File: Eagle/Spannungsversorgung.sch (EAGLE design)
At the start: 2 parts

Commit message: Added PinHeads to the Eagle file
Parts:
- added JP1, JP2: (no value), pinhead:PINHD-1X22
- added U1: ESP32-S2-SAOLA-1R, ESP32-S2-SAOLA-1R:ESP32-S2-SAOLA-1R
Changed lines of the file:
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@@
 <setting verticaltext="up"/>
 </settings>
-<grid distance="0.1" unitdist="inch" unit="mil" style="lines" multiple="1" display="yes" altdistance="0.01" altunitdist="inch" altunit="inch"/>
+<grid distance="0.1" unitdist="inch" unit="inch" style="lines" multiple="1" display="no" altdistance="0.01" altunitdist="inch" altunit="inch"/>
 <layers>
 <layer number="1" name="Top" color="4" fill="1" visible="no" active="no"/>
@@
 <part name="GND2" library="supply1" library_urn="urn:adsk.eagle:library:371" deviceset="GND" device=""/>
 <part name="FRAME1" library="frames" library_urn="urn:adsk.eagle:library:229" deviceset="A4L-LOC" device=""/>
+<part name="JP1" library="pinhead" library_urn="urn:adsk.eagle:library:325" deviceset="PINHD-1X22" device="" package3d_urn="urn:adsk.eagle:package:22442/3"/>
+<part name="JP2" library="pinhead" library_urn="urn:adsk.eagle:library:325" deviceset="PINHD-1X22" device="" package3d_urn="urn:adsk.eagle:package:22442/3"/>
+<part name="U1" library="ESP32-S2-SAOLA-1R" deviceset="ESP32-S2-SAOLA-1R" device=""/>
+<part name="FRAME2" library="frames" library_urn="urn:adsk.eagle:library:229" deviceset="A4L-LOC" device=""/>
+<part name="FRAME3" library="frames" library_urn="urn:adsk.eagle:library:229" deviceset="A4L-LOC" device=""/>
 </parts>
 <sheets>
+<sheet>
+<description>PINs</description>
+<plain>
+</plain>
+<instances>
+<instance part="JP1" gate="A" x="20.32" y="55.88" smashed="yes">
+<attribute name="NAME" x="13.97" y="84.455" size="1.778" layer="95"/>
+<attribute name="VALUE" x="13.97" y="22.86" size="1.778" layer="96"/>
+</instance>
+<instance part="JP2" gate="A" x="50.8" y="55.88" smashed="yes">
+<attribute name="NAME" x="44.45" y="84.455" size="1.778" layer="95"/>
+<attribute name="VALUE" x="44.45" y="22.86" size="1.778" layer="96"/>
+</instance>
+<instance part="FRAME2" gate="G$1" x="0" y="0" smashed="yes">
+<attribute name="DRAWING_NAME" x="217.17" y="15.24" size="2.54" layer="94"/>
+<attribute name="LAST_DATE_TIME" x="217.17" y="10.16" size="2.286" layer="94"/>
+<attribute name="SHEET" x="230.505" y="5.08" size="2.54" layer="94"/>
+</instance>
+</instances>
+<busses>
+</busses>
+<nets>
+</nets>
+</sheet>
 <sheet>
 <description>Spannungsregler</description>
@@
 </nets>
 </sheet>
+<sheet>
+<description>Verschiedenes</description>
+<plain>
+</plain>
+<instances>
+<instance part="U1" gate="G$1" x="73.66" y="58.42" smashed="yes">
+<attribute name="NAME" x="58.42" y="93.98" size="1.778" layer="95" align="top-left"/>
+<attribute name="VALUE" x="58.42" y="22.86" size="1.778" layer="96"/>
+</instance>
+<instance part="FRAME3" gate="G$1" x="0" y="0" smashed="yes">
+<attribute name="DRAWING_NAME" x="217.17" y="15.24" size="2.54" layer="94"/>
+<attribute name="LAST_DATE_TIME" x="217.17" y="10.16" size="2.286" layer="94"/>
+<attribute name="SHEET" x="230.505" y="5.08" size="2.54" layer="94"/>
+</instance>
+</instances>
+<busses>
+</busses>
+<nets>
+</nets>
+</sheet>

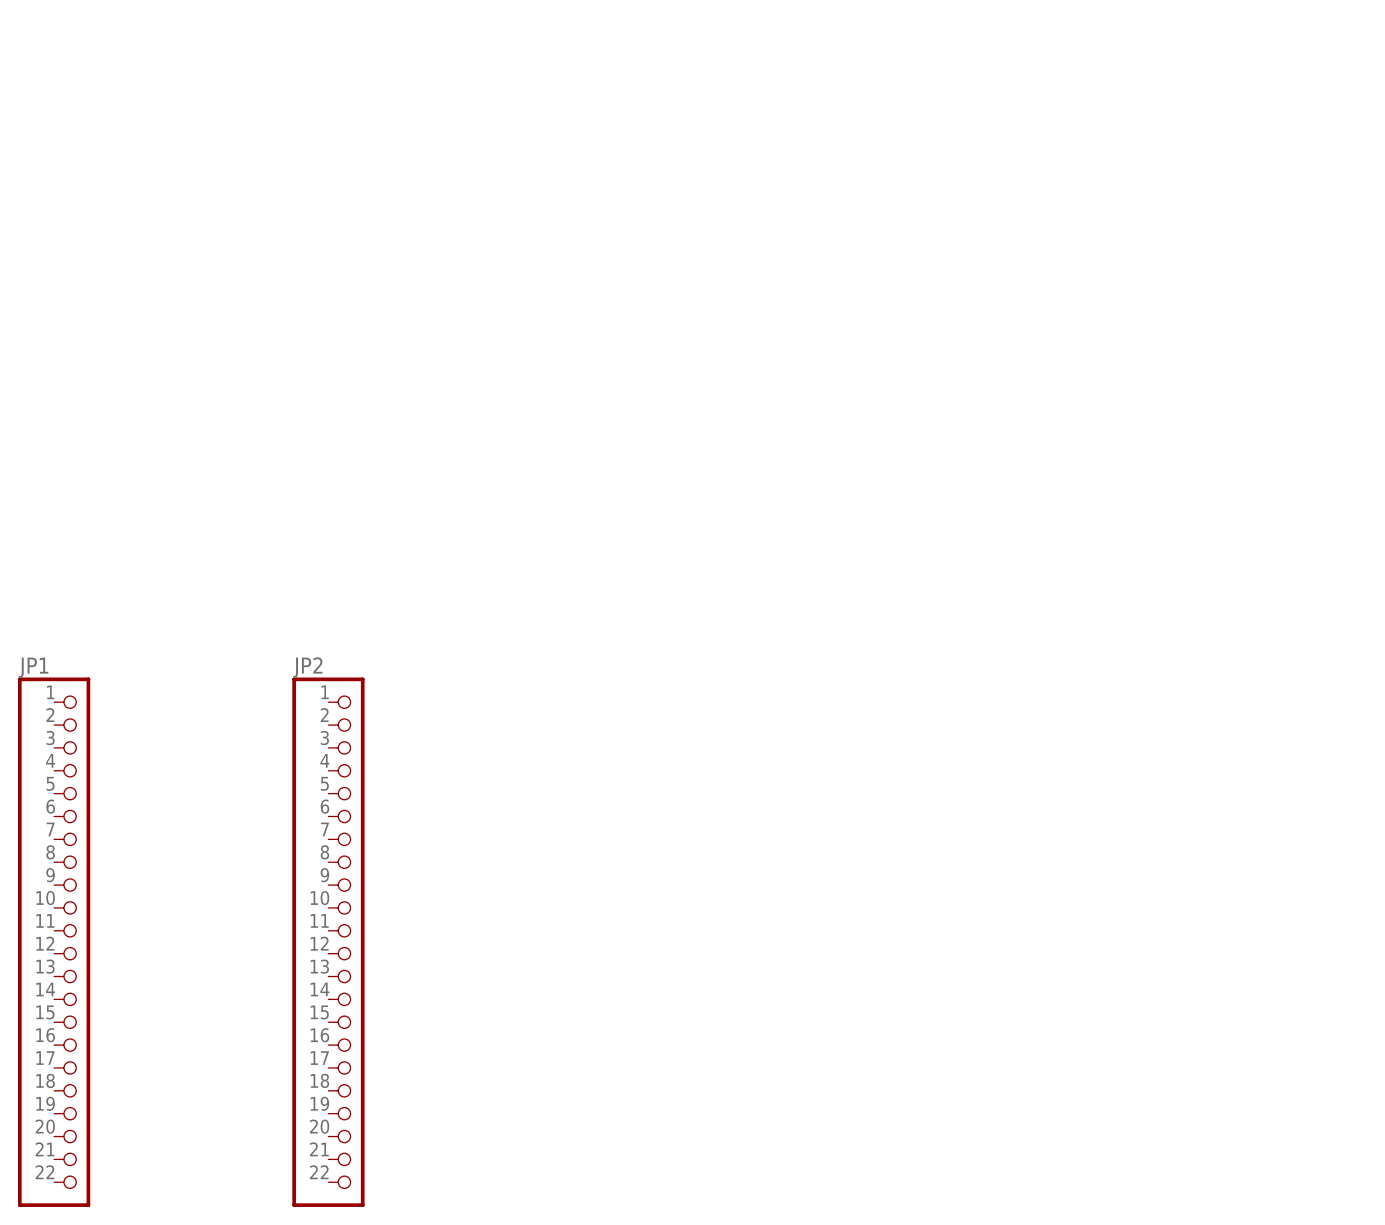
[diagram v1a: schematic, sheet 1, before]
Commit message: Added Features & Verwendung to the documentation of LT1529-5
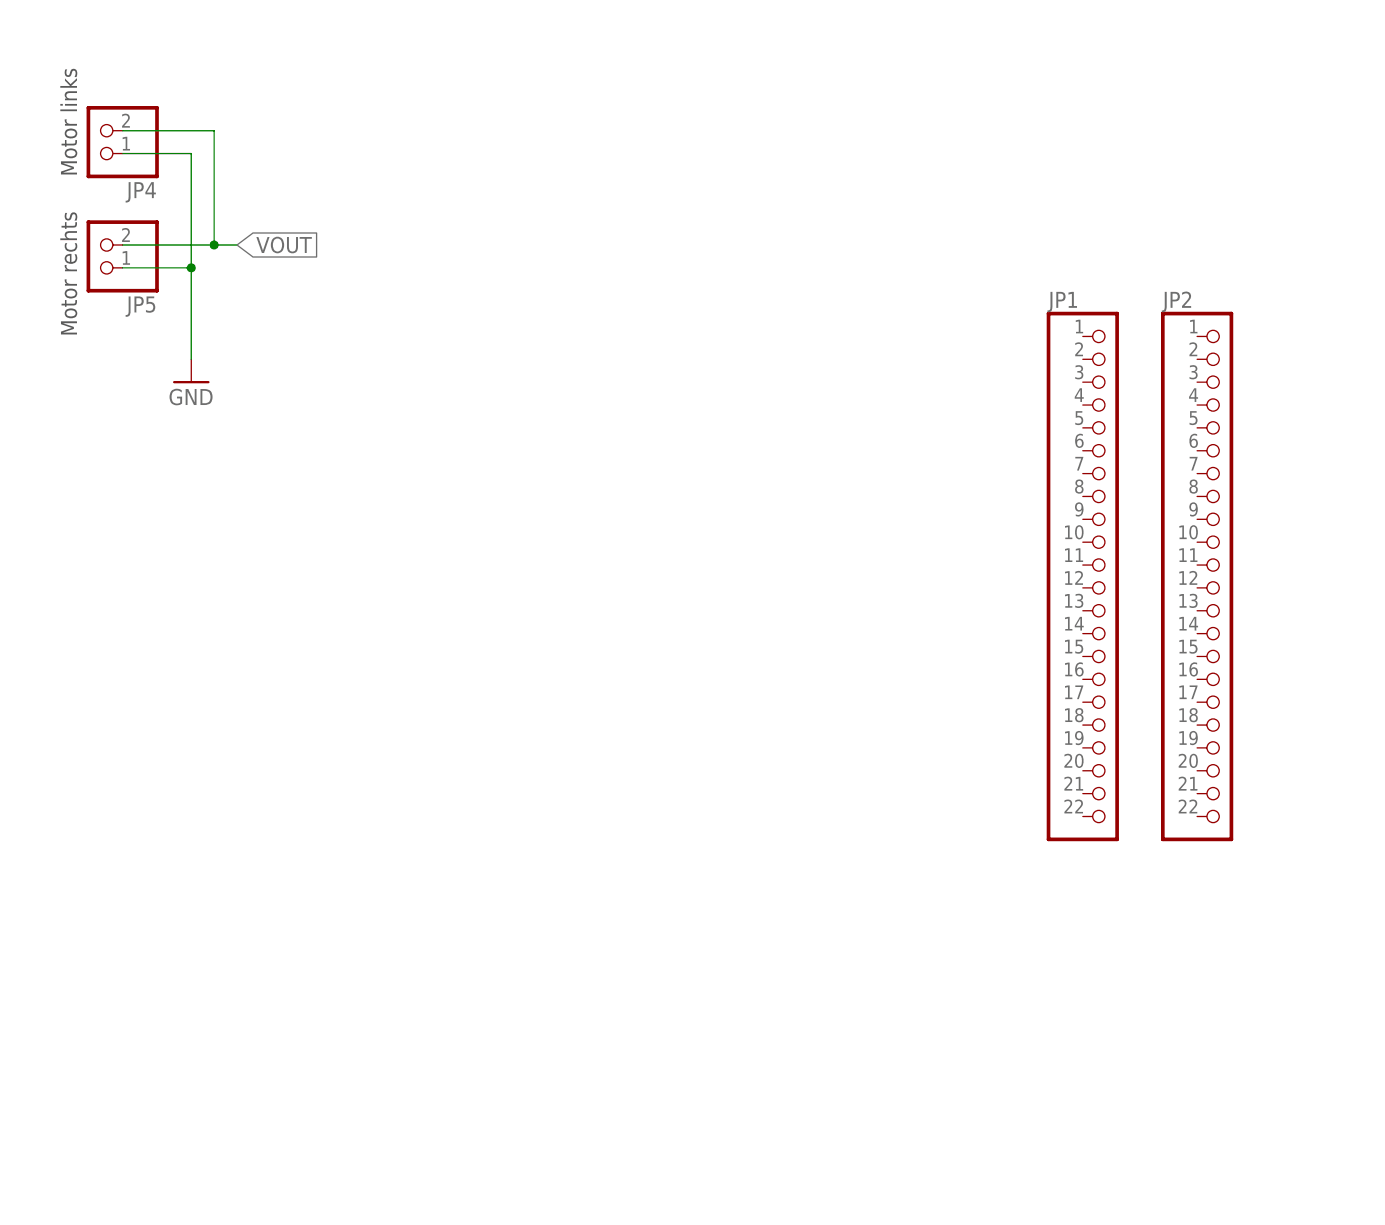
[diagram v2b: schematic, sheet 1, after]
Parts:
- removed U1: ESP32-S2-SAOLA-1R, ESP32-S2-SAOLA-1R:ESP32-S2-SAOLA-1R
- added D1: 1N5400, diode:1N5400
- added JP3, JP4, JP5: (no value), pinhead:PINHD-1X2
- added S1: (no value), switch-dil:DS01
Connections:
- new net N$2: D1.C, IC1.IN
- net BATTERY: now also D1.A, JP3.2, S1.1, S1.2; no longer IC1.IN
- net GND: now also JP3.1, JP4.1, JP5.1
- net VOUT: now also JP4.2, JP5.2
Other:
- note added: "Batterie"
- note added: "Motor links"
- note added: "Motor rechts"
- moved on the sheet: JP1, JP2
